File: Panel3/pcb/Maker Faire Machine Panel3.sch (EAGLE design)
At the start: 22 parts, among them IC1 TJA1049

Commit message: Add 2nd CAN terminal block for ease of wiring
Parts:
- added JP8: (no value), SparkFun-Connectors:M023.5MM
- renumbered JP3 to JP9
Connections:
- net CANH: now also JP8.1
- net CANL: now also JP8.2
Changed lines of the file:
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@@
 </part>
 <part name="GND7" library="SparkFun-Aesthetics" deviceset="GND" device=""/>
-<part name="JP3" library="SparkFun-Connectors" deviceset="M02" device="3.5MM"/>
+<part name="JP9" library="SparkFun-Connectors" deviceset="M02" device="3.5MM"/>
 <part name="JP4" library="SparkFun-Connectors" deviceset="M04" device="SCREW"/>
 <part name="JP5" library="SparkFun-Connectors" deviceset="M04" device="SCREW"/>
@@
 <part name="SUPPLY5" library="SparkFun-Aesthetics" deviceset="5V" device=""/>
 <part name="GND10" library="SparkFun-Aesthetics" deviceset="GND" device=""/>
+<part name="JP8" library="SparkFun-Connectors" deviceset="M02" device="3.5MM"/>
 </parts>
 <sheets>
@@
 </instance>
 <instance part="GND7" gate="1" x="180.34" y="-40.64"/>
-<instance part="JP3" gate="G$1" x="251.46" y="-43.18" rot="R180"/>
+<instance part="JP9" gate="G$1" x="251.46" y="-43.18" rot="R180"/>
 <instance part="JP4" gate="G$1" x="106.68" y="-30.48" rot="R180"/>
 <instance part="JP5" gate="G$1" x="106.68" y="-55.88" rot="R180"/>
@@
 <instance part="SUPPLY5" gate="G$1" x="99.06" y="20.32"/>
 <instance part="GND10" gate="1" x="99.06" y="12.7"/>
+<instance part="JP8" gate="G$1" x="251.46" y="-30.48" rot="R180"/>
 </instances>
 <busses>
@@
 <segment>
 <pinref part="IC1" gate="G$1" pin="CANH"/>
-<wire x1="213.36" y1="-43.18" x2="243.84" y2="-43.18" width="0.1524" layer="91"/>
+<wire x1="213.36" y1="-43.18" x2="241.3" y2="-43.18" width="0.1524" layer="91"/>
 <label x="233.68" y="-43.18" size="1.778" layer="95"/>
-<pinref part="JP3" gate="G$1" pin="1"/>
+<pinref part="JP9" gate="G$1" pin="1"/>
+<pinref part="JP8" gate="G$1" pin="1"/>
+<wire x1="241.3" y1="-43.18" x2="243.84" y2="-43.18" width="0.1524" layer="91"/>
+<wire x1="243.84" y1="-30.48" x2="241.3" y2="-30.48" width="0.1524" layer="91"/>
+<wire x1="241.3" y1="-30.48" x2="241.3" y2="-43.18" width="0.1524" layer="91"/>
+<junction x="241.3" y="-43.18"/>
 </segment>
 </net>
@@
 <wire x1="213.36" y1="-45.72" x2="243.84" y2="-45.72" width="0.1524" layer="91"/>
 <label x="233.68" y="-45.72" size="1.778" layer="95"/>
-<pinref part="JP3" gate="G$1" pin="2"/>
-</segment>
-</net>
+<pinref part="JP9" gate="G$1" pin="2"/>
+<pinref part="JP8" gate="G$1" pin="2"/>
+<wire x1="243.84" y1="-33.02" x2="243.84" y2="-45.72" width="0.1524" layer="91"/>
+<junction x="243.84" y="-45.72"/>
+</segment>
+</net>

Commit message: Increase cutoff frequency of ball detector lowpass
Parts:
- C1, C2: value 0.1uF -> 0.01uF
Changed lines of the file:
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@@
 <part name="GND1" library="SparkFun-Aesthetics" deviceset="GND" device=""/>
 <part name="R1" library="SparkFun-Passives" deviceset="RESISTOR" device="1206" value="1k"/>
-<part name="C1" library="SparkFun-Passives" deviceset="CAP" device="1206" value="0.1uF"/>
+<part name="C1" library="SparkFun-Passives" deviceset="CAP" device="1206" value="0.01uF"/>
 <part name="R2" library="SparkFun-Passives" deviceset="RESISTOR" device="1206" value="1k"/>
 <part name="GND2" library="SparkFun-Aesthetics" deviceset="GND" device=""/>
 <part name="GND3" library="SparkFun-Aesthetics" deviceset="GND" device=""/>
 <part name="R3" library="SparkFun-Passives" deviceset="POTENTIOMETER" device="" value="2k"/>
-<part name="C2" library="SparkFun-Passives" deviceset="CAP" device="1206" value="0.1uF"/>
+<part name="C2" library="SparkFun-Passives" deviceset="CAP" device="1206" value="0.01uF"/>
 <part name="R4" library="SparkFun-Passives" deviceset="RESISTOR" device="1206" value="1k"/>
 <part name="GND4" library="SparkFun-Aesthetics" deviceset="GND" device=""/>

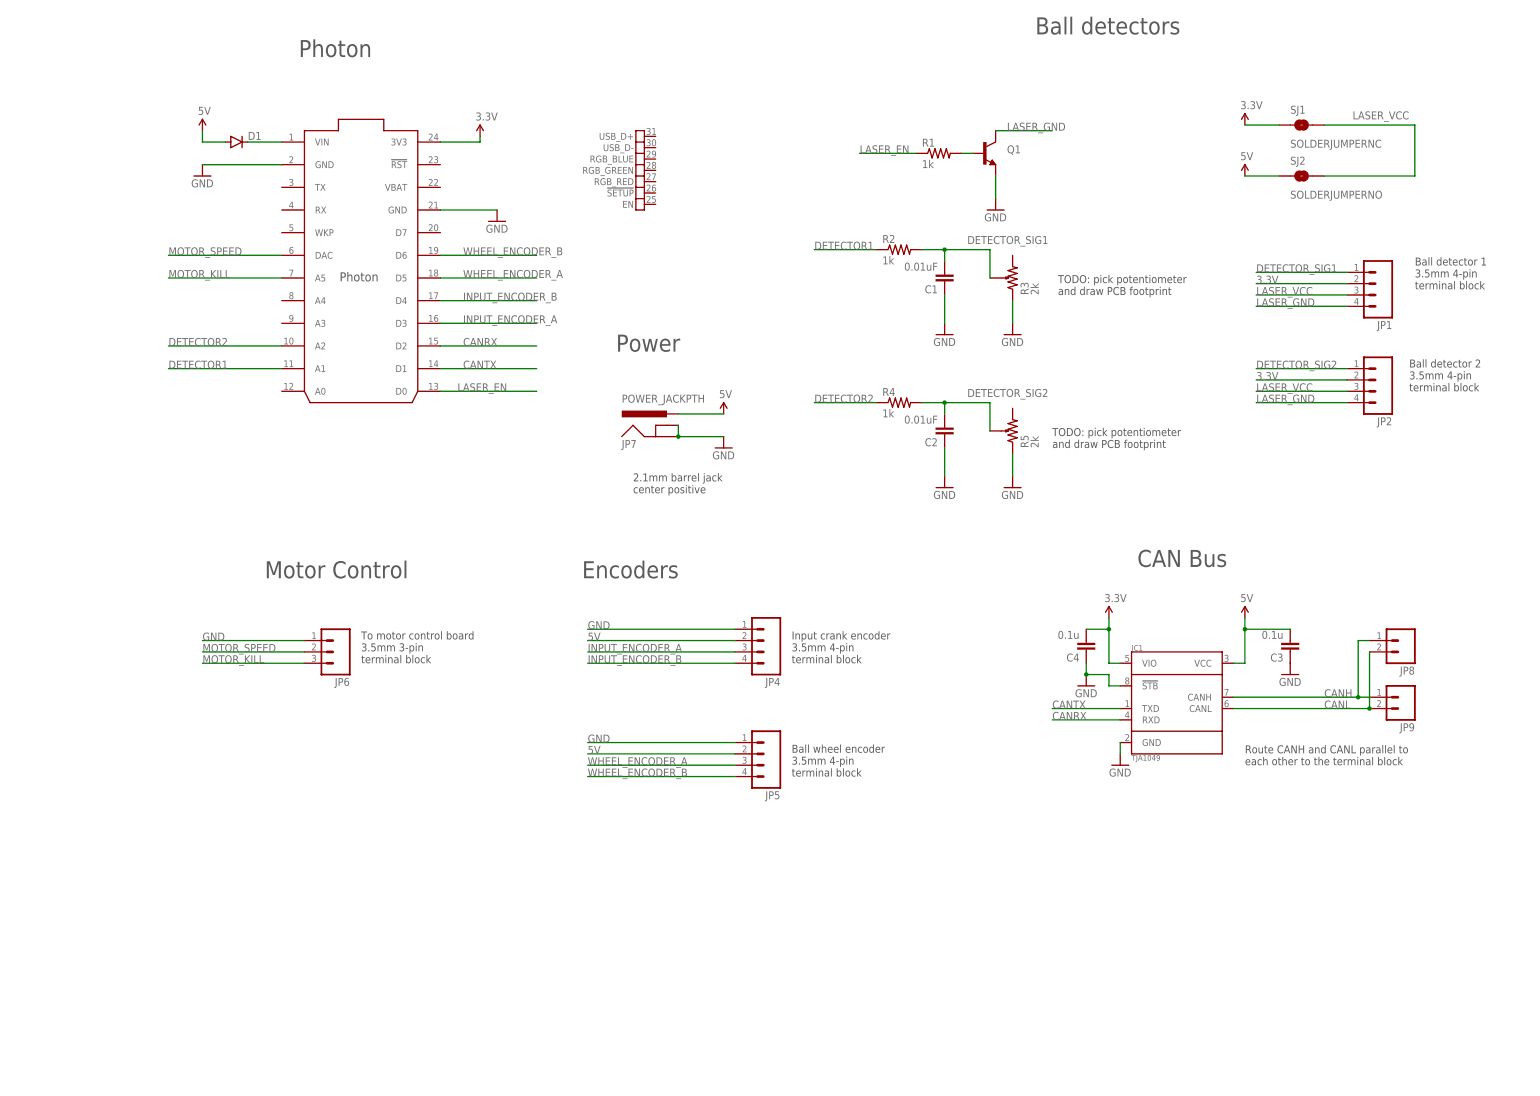
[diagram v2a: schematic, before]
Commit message: Finished Panel 3 PCB Layout
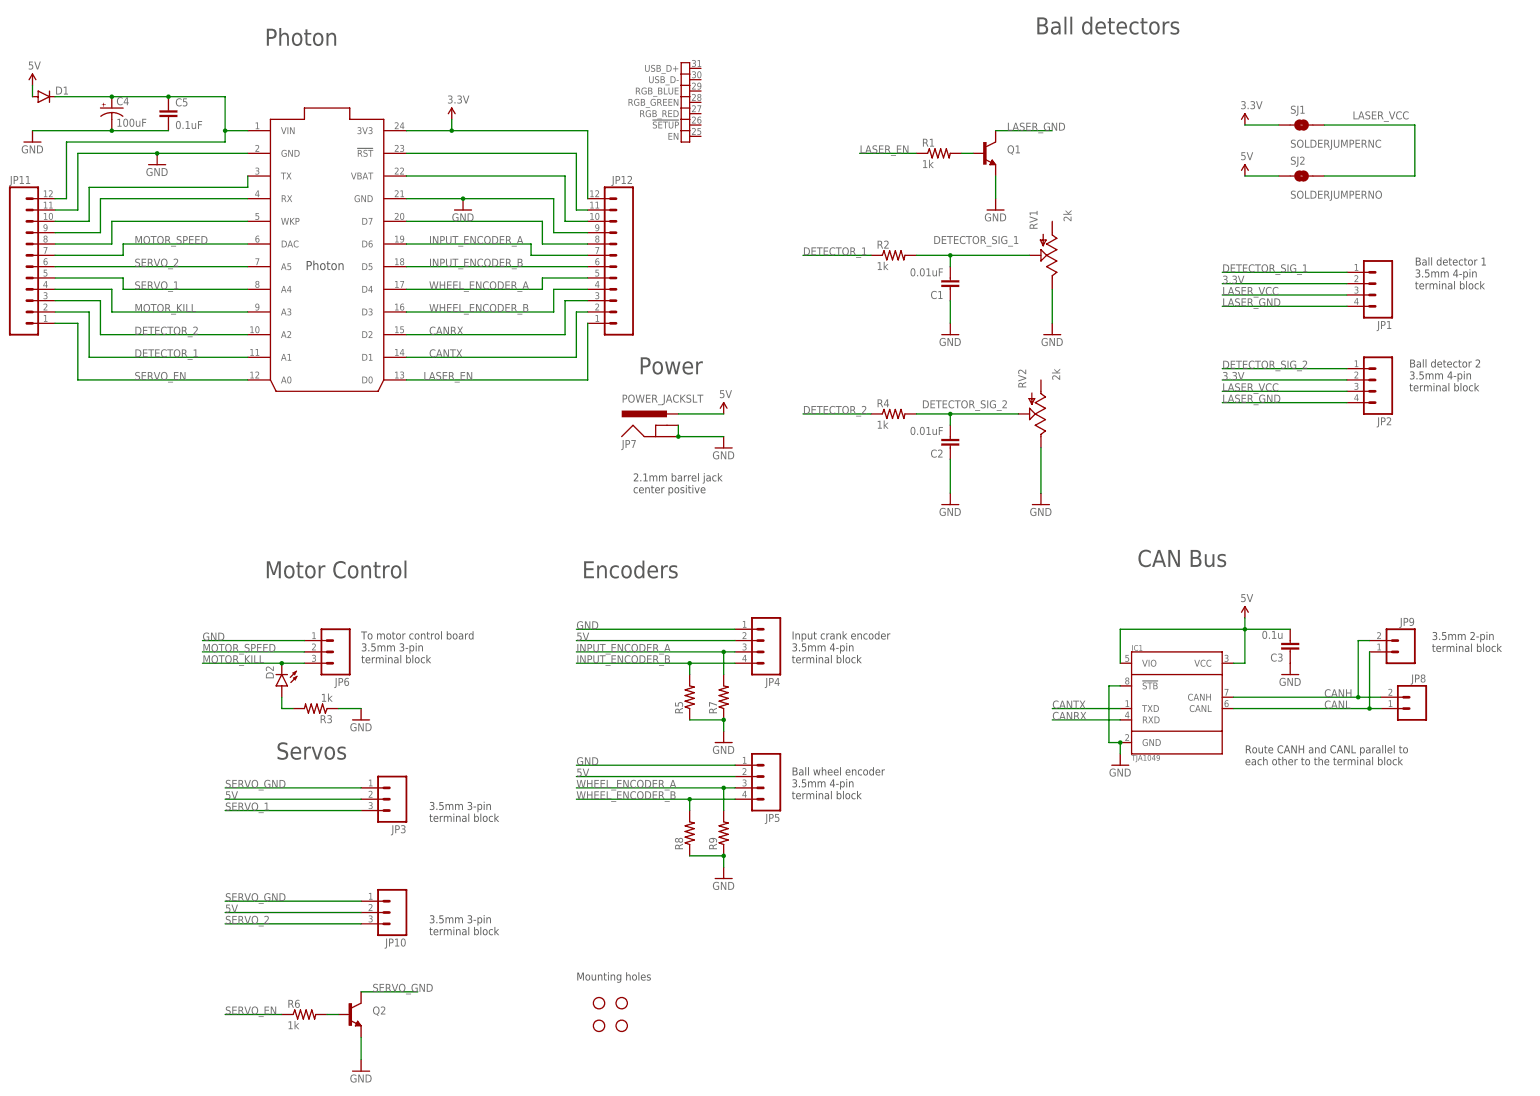
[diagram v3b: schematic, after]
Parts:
- added C5: 0.1uF, SparkFun-Capacitors:CAP1206
- added D2: (no value), SparkFun-LED:LED5MM
- added JP10, JP3: (no value), SparkFun-Connectors:M03SCREW
- added JP11, JP12: (no value), SparkFun-Connectors:M12NO_SILK
- added Q2: (no value), SparkFun-DiscreteSemi:TRANSISTOR_NPNTO92
- added R6: 1k, SparkFun-Passives:RESISTOR1206
- added R7, R8, R9: (no value), SparkFun-Resistors:RESISTORKIT
- added RV1, RV2: 2k, SparkFun-Electromechanical:POT100K_3362U
- added STANDOFF1, STANDOFF2, STANDOFF3, STANDOFF4: STAND-OFF, SparkFun-Electromechanical:STAND-OFF
- C1, C2: PARTNO (none) -> 12065C103KAT2A
- C3: device rcl:C-EUC1206 -> SparkFun-Capacitors:CAP1206
- C4: value 0.1u -> 100uF; device rcl:C-EUC1206 -> SparkFun-Capacitors:CAP_POLPTH1; PARTNO 12065C104KAT2A -> EEU-FM1H101B
- D1: PARTNO (none) -> B230A-13-F
- JP1, JP2, JP4: PARTNO (none) -> OSTTE040104
- JP5: PARTNO (none) -> OSTTE030104
- JP6, JP8, JP9: PARTNO (none) -> OSTTE020104
- JP7: value POWER_JACKPTH -> POWER_JACKSLT; device SparkFun-Connectors:POWER_JACKPTH -> SparkFun-Connectors:POWER_JACKSLT; PARTNO (none) -> PJ-202A
- Q1: PARTNO (none) -> PN2222ABU
- R1, R2, R4: PARTNO (none) -> ERJ-8ENF1001V
- R3: value 2k -> 1k; device SparkFun-Passives:POTENTIOMETER -> SparkFun-Passives:RESISTOR1206; PARTNO (none) -> ERJ-8ENF1001V
- R5: value 2k -> (none); device SparkFun-Passives:POTENTIOMETER -> SparkFun-Resistors:RESISTORKIT; BOM (none) -> EXCLUDE
- SJ1, SJ2: BOM (none) -> EXCLUDE
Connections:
- removed net DETECTOR1: R2.1, U$1G$1.A1
- removed net DETECTOR2: R4.1, U$1G$1.A2
- removed net DETECTOR_SIG1: C1.2, JP1.1, R2.2, R3.P$1
- removed net DETECTOR_SIG2: C2.2, JP2.1, R4.2, R5.P$1
- removed net N$2: D1.C, U$1G$1.VIN
- removed net N$3: U$1G$1.GND@2
- new net DETECTOR_1: JP11.2, R2.1, U$1G$1.A1
- new net DETECTOR_2: JP11.3, R4.1, U$1G$1.A2
- new net DETECTOR_SIG_1: C1.2, JP1.1, R2.2, RV1.S
- new net DETECTOR_SIG_2: C2.2, JP2.1, R4.2, RV2.S
- new net N$11: JP12.8, U$1G$1.D7
- new net N$13: JP12.10, U$1G$1.VBAT
- new net N$14: JP12.11, U$1G$1.!RST
- new net N$4: Q2.B, R6.2
- new net N$5: D2.A, R3.2
- new net RX: JP11.9, U$1G$1.RX
- new net SERVO_1: JP11.5, JP3.3, U$1G$1.A4
- new net SERVO_2: JP10.3, JP11.6, U$1G$1.A5
- new net SERVO_EN: JP11.1, R6.1, U$1G$1.A0
- new net SERVO_GND: JP10.1, JP3.1, Q2.C
- new net TX: JP11.10, U$1G$1.TX
- new net VIN: C4.+, C5.1, D1.C, JP11.12, U$1G$1.VIN
- new net WKP: JP11.8, U$1G$1.WKP
- net 3.3V: now also JP12.12; no longer C4.2, IC1.VIO
- net 5V: now also IC1.VIO, JP10.2, JP3.2
- net CANH: now also JP8.2, JP9.2; no longer JP8.1, JP9.1
- net CANL: now also JP8.1, JP9.1; no longer JP8.2, JP9.2
- net CANRX: now also JP12.3
- net CANTX: now also JP12.2
- net GND: now also C4.-, C5.2, JP11.11, JP12.9, Q2.E, R7.1, R8.1, R9.1, RV1.E, RV2.E, U$1G$1.GND@2; no longer C4.1
- net INPUT_ENCODER_A: now also JP12.7, R7.2, U$1G$1.D6; no longer U$1G$1.D3
- net INPUT_ENCODER_B: now also JP12.6, R5.2, U$1G$1.D5; no longer U$1G$1.D4
- net LASER_EN: now also JP12.1
- net MOTOR_KILL: now also D2.C, JP11.4, U$1G$1.A3; no longer U$1G$1.A5
- net MOTOR_SPEED: now also JP11.7
- net WHEEL_ENCODER_A: now also JP12.5, R9.2, U$1G$1.D4; no longer U$1G$1.D5
- net WHEEL_ENCODER_B: now also JP12.4, R8.2, U$1G$1.D3; no longer U$1G$1.D6
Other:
- note added: "3.5mm 2-pin terminal block"
- note added: "3.5mm 3-pin terminal block"
- note added: "Mounting holes"
- note added: "Servos"
- note removed: "TODO: pick potentiometer and draw PCB footprint"
- moved on the sheet: C1, C2, D1, JP5, JP8, JP9, R2, R4
